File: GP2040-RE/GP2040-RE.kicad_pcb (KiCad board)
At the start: 2 copper layers, 47.5 x 32.9 mm, 38 parts, among them J1 I2C Slave, J2 DEBUG, J3 USB Programming, J4 Console, SW1 BOOTSEL, SW2 RESET, U1 W25Q16JV, U2 RP2040, U3 RT6154AGQW

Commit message: Much happier now
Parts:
- removed SW1: BOOTSEL, Button_Switch_SMD:SW_SPST_B3S-1000
- removed SW2: RESET, Button_Switch_SMD:SW_SPST_B3S-1000
- added J5: RJ-45, RJ-45:CONN8_2-908LF_AMP, F.Cu at (130.3, 101.4)
- added J6: I2C Passthrough, JST-SH:JST_SH_SM04B-SRSS-TB_1x04-1MP_P1.00mm_Horizontal, F.Cu at (146.9, 84.8)
- added J7: Micro_SD_Card, microSD:MEM2061-01-188-00-A_GCT, F.Cu at (126.5, 89.9)
- added J8: Conn_01x10, Connector_PinHeader_2.54mm:PinHeader_1x10_P2.54mm_Vertical, F.Cu at (167.0, 112.3)
- added S1: BOOTSEL, EVP_BB2A9B000:SW_EVP-BB2A9B000, F.Cu at (163.1, 106.5)
- added S2: RESET, EVP_BB2A9B000:SW_EVP-BB2A9B000, F.Cu at (159.4, 106.5)
- J1: footprint Connector_JST:JST_PH_S4B-PH-K_1x04_P2.00mm_Horizontal -> JST-SH:JST_SH_SM04B-SRSS-TB_1x04-1MP_P1.00mm_Horizontal
- J2: footprint Connector_PinHeader_2.54mm:PinHeader_1x03_P2.54mm_Vertical -> JST-SH:JST_SH_SM03B-SRSS-TB_1x03-1MP_P1.00mm_Horizontal
- U1: footprint Package_SO:SOIC-8_5.23x5.23mm_P1.27mm -> W25Q16:USON-8_UX_2x3x0p6_WIN
- moved J2 8.83 mm to (160.4, 111.2), turned to 0 degrees
- moved R1 5.06 mm to (146.1, 93.2)
- moved C2 3.62 mm to (150.7, 92.3)
- moved C1 3.61 mm to (149.9, 92.3)
- moved U1 3.44 mm to (148.7, 94.8)
- moved J1 2.57 mm to (139.1, 84.8)
- moved R5 1.08 mm to (139.3, 88.7)
- moved C8 0.85 mm to (150.8, 98.2)
- moved R4 0.35 mm to (140.9, 88.7)
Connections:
- U2 pad 11: /NES -> unconnected-(U2-GPIO8-Pad11)
- U2 pad 12: /SNES -> unconnected-(U2-GPIO9-Pad12)
- U2 pad 13: /N64 -> unconnected-(U2-GPIO10-Pad13)
- U2 pad 14: /GC -> unconnected-(U2-GPIO11-Pad14)
- U2 pad 16: unconnected-(U2-GPIO13-Pad16) -> /SPI1_CSn
- U2 pad 34: unconnected-(U2-GPIO22-Pad34) -> /OCS
- U2 pad 35: unconnected-(U2-GPIO23-Pad35) -> /RESET
- U2 pad 36: unconnected-(U2-GPIO24-Pad36) -> /Data_Command
- U2 pad 38: unconnected-(U2-GPIO26_ADC0-Pad38) -> /SPI1_SCK
- U2 pad 39: unconnected-(U2-GPIO27_ADC1-Pad39) -> /SPI1_TX_MOSI
- U2 pad 40: unconnected-(U2-GPIO28_ADC2-Pad40) -> /SPI1_RX_MISO
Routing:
- net /CD_gpio: track 13.4 -> 73.7 mm, vias 0 -> 2
- net /CMD_gpio: track 8.56 -> 64.3 mm, vias 0 -> 2
- net /D2_gpio: track 7.20 -> 61.9 mm, vias 0 -> 2
- net /CLK_gpio: track 9.92 -> 64.3 mm, vias 0 -> 2
- net /D1_gpio: track 7.42 -> 61.0 mm, vias 0 -> 2
- net /D0_gpio: track 7.61 -> 61.0 mm, vias 0 -> 2
- net /D3_gpio: track 7.14 -> 58.9 mm, vias 0 -> 2
- net +3.3V: track 96.9 -> 126.4 mm, vias 12 -> 14
- net Net-(R1-Pad1): track 53.9 -> 37.2 mm
- net GND: track 26.6 -> 40.7 mm, vias 12 -> 30
- net /RUN: track 16.1 -> 2.61 mm
- net /SPI1_RX_MISO: track 0.00 -> 12.6 mm, vias 0 -> 1
- net /GreenStripe: track 16.9 -> 27.9 mm
- net /OrangeSolid: track 17.9 -> 27.6 mm
- net /SPI1_TX_MOSI: track 0.00 -> 9.59 mm, vias 0 -> 1
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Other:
- board size 47.5 x 32.9 mm -> 50.8 x 33 mm

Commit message: Now with blinky lights
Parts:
- added D3: LED_Small, LED_SMD:LED_0201_0603Metric, F.Cu at (140.7, 112.8)
- added D4: LED_Small, LED_SMD:LED_0201_0603Metric, F.Cu at (140.7, 113.7)
- added Q1: SBC846BWT1G, SBC846BW:SOT-323-3_2P2X1P35_ONS, F.Cu at (149.0, 111.0)
- added R10: 10k, Resistor_SMD:R_0201_0603Metric, F.Cu at (146.2, 113.7)
- added R11: 10k, Resistor_SMD:R_0201_0603Metric, F.Cu at (142.1, 113.7)
- added R12: 10k, Resistor_SMD:R_0201_0603Metric, F.Cu at (142.1, 112.8)
- added U4: TPS3702CX50DDCR, TPS3702CX50:DDC0006A_N, F.Cu at (145.2, 111.2)
- moved C14 1.62 mm to (148.4, 107.8)
- moved C10 1.59 mm to (150.6, 101.9)
- moved U3 1.47 mm to (145.2, 106.3)
- moved L1 1.46 mm to (145.2, 102.6)
- moved R9 1.13 mm to (142.8, 106.6)
- moved R8 1.12 mm to (142.8, 108.0)
- moved R6 0.96 mm to (148.4, 107.1), turned to 180 degrees
- moved C15 0.69 mm to (148.4, 105.0)
- moved C16 0.69 mm to (148.4, 105.7)
- moved R7 0.69 mm to (148.4, 106.4)
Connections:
- net Net-(D1-Pad1) renamed /InputVoltage
- J8 pad 2: +3.3V -> Net-(J8-Pin_2)
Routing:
- net /CD_gpio: track 73.7 -> 34.2 mm
- net Net-(J8-Pin_2): track 0.00 -> 18.3 mm, vias 0 -> 1
- net VBUS: track 31.0 -> 45.4 mm, vias 1 -> 2
- net /5V_EN: track 0.00 -> 11.0 mm
- net +3.3V: track 126.4 -> 136.6 mm, vias 14 -> 15
- net /InputVoltage: track 6.92 -> 12.1 mm
- net /BrownStripe: track 30.9 -> 34.6 mm
- net /GreenSolid: track 27.3 -> 30.3 mm
- net /BlueStripe: track 28.3 -> 31.3 mm
- net /BlueSolid: track 25.0 -> 27.9 mm
- net GND: track 40.7 -> 43.1 mm, vias 30 -> 34
- net /GreenStripe: track 27.9 -> 29.7 mm
- net Net-(D4-A): track 0.00 -> 0.76 mm
- net Net-(D3-A): track 0.00 -> 0.76 mm
- net Net-(U3-VINA): track 0.96 -> 1.61 mm
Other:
- board size 50.8 x 33 mm -> 50.8 x 33.2 mm

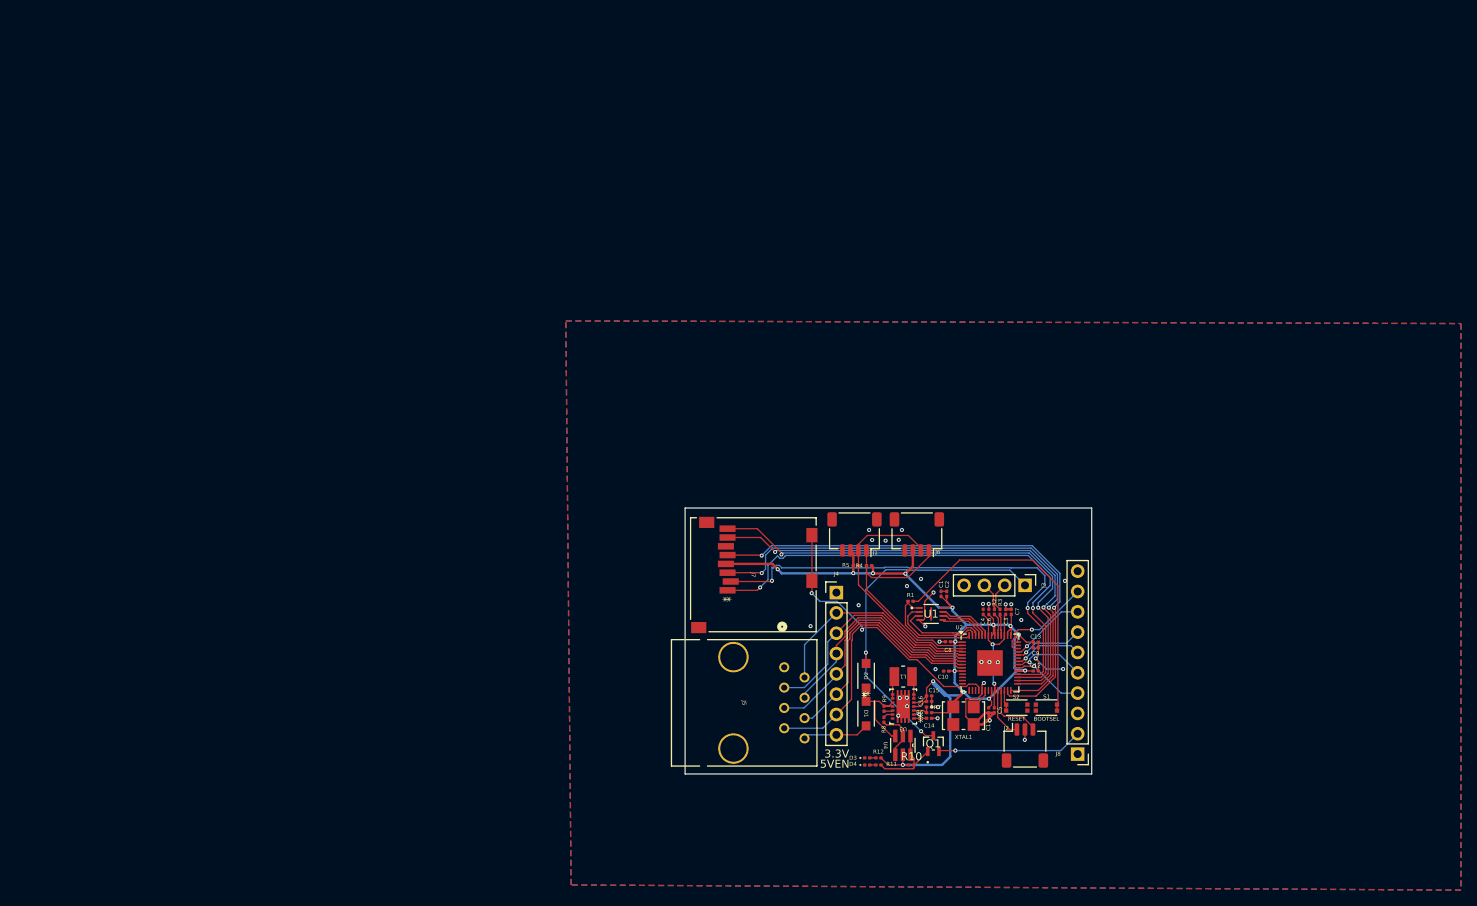
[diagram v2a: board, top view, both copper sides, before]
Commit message: rebuilding part libraries
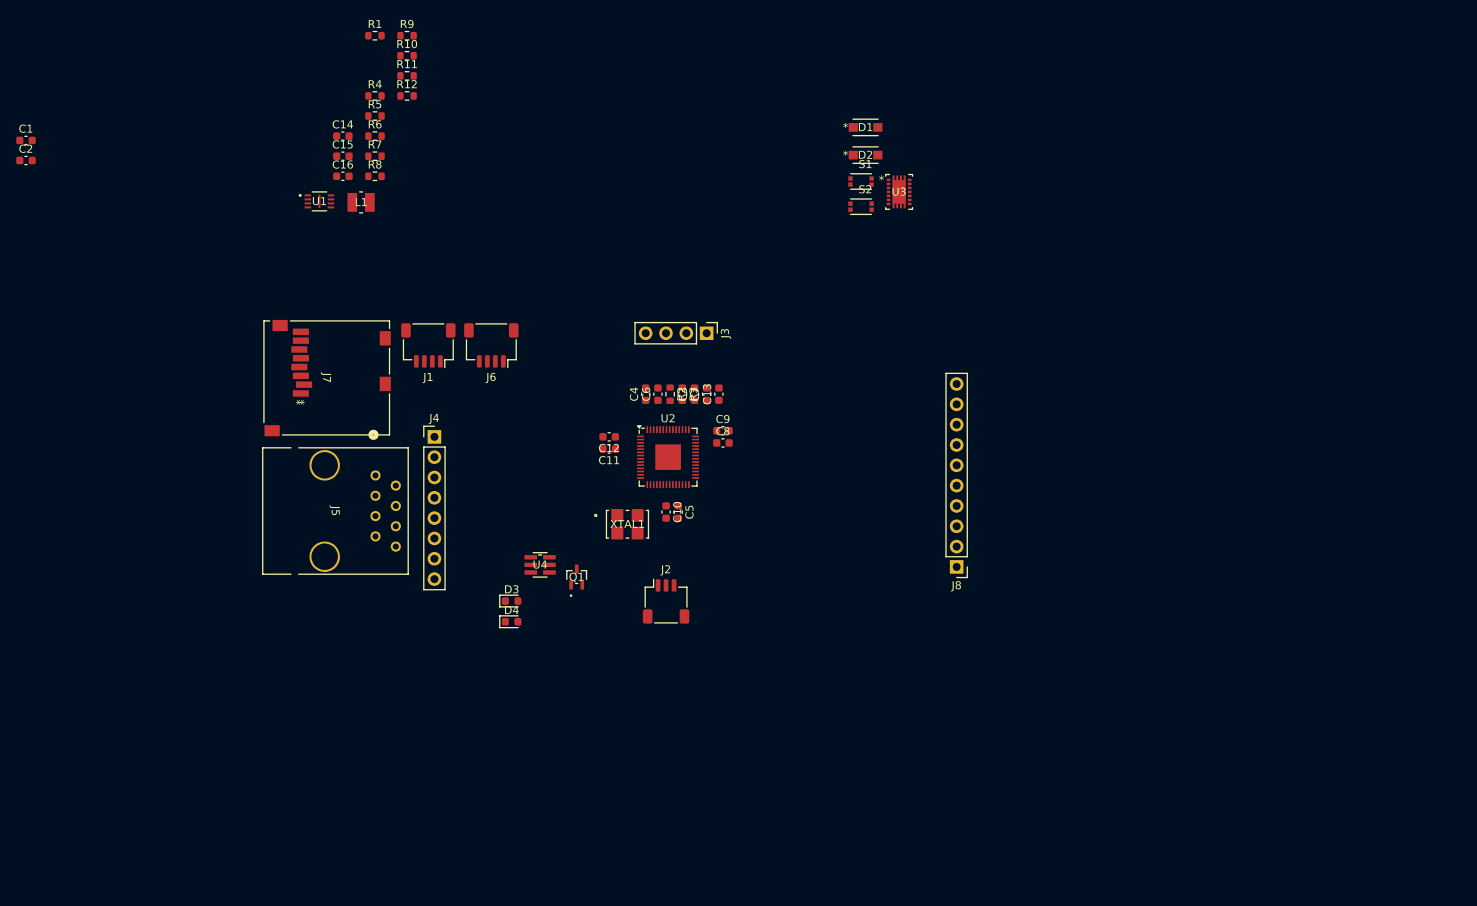
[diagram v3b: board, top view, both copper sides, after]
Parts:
- C1, C10, C11, C12, C13, C14, C15, C16, C2, C3, C4, C5, C6, C7, C8, C9: footprint Capacitor_SMD:C_0201_0603Metric -> Capacitor_SMD:C_0603_1608Metric
- D3, D4: footprint LED_SMD:LED_0201_0603Metric -> LED_SMD:LED_0603_1608Metric
- R1, R10, R11, R12, R2, R3, R4, R5, R6, R7, R8, R9: footprint Resistor_SMD:R_0201_0603Metric -> Resistor_SMD:R_0603_1608Metric
- moved C1 127.7 mm to (35.6, 35.6), turned to 0 degrees
- moved C2 127.2 mm to (35.6, 38.1), turned to 0 degrees
- moved R10 108.8 mm to (83.2, 25.0)
- moved R11 104.4 mm to (83.2, 27.5), turned to 0 degrees
- moved C14 103.3 mm to (75.2, 35.1)
- moved R9 103.1 mm to (83.2, 22.5), turned to 0 degrees
- moved R12 101.6 mm to (83.2, 30.0), turned to 0 degrees
- moved R6 100.0 mm to (79.2, 35.1), turned to 0 degrees
- moved C15 99.6 mm to (75.2, 37.6)
- moved C16 98.4 mm to (75.2, 40.1)
- moved R7 97.7 mm to (79.2, 37.6)
- moved R1 97.4 mm to (79.2, 22.5), turned to 0 degrees
- moved R8 93.1 mm to (79.2, 40.1), turned to 0 degrees
- moved U1 92.2 mm to (72.2, 43.2)
- moved L1 90.0 mm to (77.4, 43.3), turned to 0 degrees
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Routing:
- net +3.3V: track 136.6 -> 0.00 mm, vias 15 -> 0
- net /CLK_gpio: track 64.3 -> 0.00 mm, vias 2 -> 0
- net /CMD_gpio: track 64.3 -> 0.00 mm, vias 2 -> 0
- net /D2_gpio: track 61.9 -> 0.00 mm, vias 2 -> 0
- net /D0_gpio: track 61.0 -> 0.00 mm, vias 2 -> 0
- net /D1_gpio: track 61.0 -> 0.00 mm, vias 2 -> 0
- net /D3_gpio: track 58.9 -> 0.00 mm, vias 2 -> 0
- net VBUS: track 45.4 -> 0.00 mm, vias 2 -> 0
- net GND: track 43.1 -> 0.00 mm, vias 34 -> 0
- net Net-(R1-Pad1): track 37.2 -> 0.00 mm
- net /BrownStripe: track 34.6 -> 0.00 mm
- net /CD_gpio: track 34.2 -> 0.00 mm, vias 2 -> 0
- net /BlueStripe: track 31.3 -> 0.00 mm
- net /SCL: track 30.6 -> 0.00 mm
- net /GreenSolid: track 30.3 -> 0.00 mm
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- removed copper zone on B.Cu, net GND
- removed copper zone on F.Cu, net GND
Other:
- board outline removed
- copper layers 2 -> 4
- rule pad_to_mask_clearance: 0.0508 -> 0.0381

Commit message: 4 Layer board
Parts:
- removed U3: RT6154AGQW, RT6154A:QFN_4AGQW_RIT
- added C17: 47u 6.3V X5R 20%, Capacitor_SMD:C_0603_1608Metric, F.Cu at (67.1, 73.7)
- added C18: 47u 6.3V X5R 20%, Capacitor_SMD:C_0603_1608Metric, F.Cu at (61.5, 72.9)
- added R13: 27 50mW 1% M0603, Resistor_SMD:R_0603_1608Metric, F.Cu at (81.5, 60.5)
- added U5: TPS3702CX50DDCR, GP2040-RE:DDC0006A_N, F.Cu at (64.3, 65.8)
- C1: value 2.2u 6.3v 20% -> 2.2u 6.3V X5R 20%
- C10, C11, C2, C4, C5, C6, C8, C9: value 100n 6.3V 10% -> 100n 6.3V X5R 10%
- C12, C13, C14: value 100n 6.3V 10% -> 2.2u 6.3V X5R 20%
- C15: value 47u 6.3V 20% -> 100n 6.3V X5R 10%
- C16: value 47u 6.3V 20% -> 47u 6.3V X5R 20%
- C3, C7: value 1uF -> 100n 6.3V X5R 10%
- D1, D2: value MBR120VLSFT1G -> LED_Small; footprint MBR120V:SDO_SOD-123FL_ONS -> LED_SMD:LED_0603_1608Metric
- D3, D4: value LED_Small -> 20V 1A; footprint LED_SMD:LED_0603_1608Metric -> GP2040-RE:SDO_SOD-123FL_ONS
- J1: value I2C Slave -> I2C Target; footprint JST-SH:JST_SH_SM04B-SRSS-TB_1x04-1MP_P1.00mm_Horizontal -> GP2040-RE:CONN_SM04B-SRSS-TB_JST
- J2: value DEBUG -> I2C Controller; footprint JST-SH:JST_SH_SM03B-SRSS-TB_1x03-1MP_P1.00mm_Horizontal -> GP2040-RE:CONN_SM04B-SRSS-TB_JST
- J3: value USB Programming -> SM03B-SRSS-TB_LF__SN_; footprint Connector_PinHeader_2.54mm:PinHeader_1x04_P2.54mm_Vertical -> GP2040-RE:JST_SM03B-SRSS-TB_LF__SN_
- J4: value Console -> USB Programming; footprint Connector_PinHeader_2.54mm:PinHeader_1x08_P2.54mm_Vertical -> Connector_PinHeader_2.54mm:PinHeader_1x04_P2.54mm_Vertical
- J5: value RJ-45 -> Conn_01x03; footprint RJ-45:CONN8_2-908LF_AMP -> Connector_PinHeader_2.54mm:PinHeader_1x03_P2.54mm_Vertical
- J6: value I2C Passthrough -> microSD; footprint JST-SH:JST_SH_SM04B-SRSS-TB_1x04-1MP_P1.00mm_Horizontal -> GP2040-RE:MEM2061-01-188-00-A_GCT
- J7: value Micro_SD_Card -> RJ-45; footprint microSD:MEM2061-01-188-00-A_GCT -> GP2040-RE:CONN8_2-908LF_AMP
- L1: value 1uH -> SRN2512-1R0M; footprint SRN2512:IND_SRN2512_BRN -> GP2040-RE:IND_SRN2512_BRN
- Q1: value SBC846BWT1G -> NPN 65V 0.1A; footprint SBC846BW:SOT-323-3_2P2X1P35_ONS -> GP2040-RE:SOT-323-3_2P2X1P35_ONS
- R11: value 10k -> VREF SHUNT 2%; footprint Resistor_SMD:R_0603_1608Metric -> GP2040-RE:DBZ3
- R12: value 10k -> 27 50mW 1% M0603
- R2, R3: value 27 50mW 1% -> 4.7k
- R4, R5: value 4.7k -> 10k
- R6: value 560K 50mW 1% -> 100K 50mW 1%
- R8: value 100K 50mW 1% -> 560K 50mW 1%
- S1: value BOOTSEL -> Buttons; footprint EVP_BB2A9B000:SW_EVP-BB2A9B000 -> GP2040-RE:SW_EVP-BB2A9B000
- S2: value RESET -> Buttons; footprint EVP_BB2A9B000:SW_EVP-BB2A9B000 -> GP2040-RE:SW_EVP-BB2A9B000
- U1: value W25Q16JV -> RP2040; footprint W25Q16:USON-8_UX_2x3x0p6_WIN -> GP2040-RE:QFN56_7X7_RPI
- U2: value RP2040 -> 16M; footprint Package_DFN_QFN:QFN-56-1EP_7x7mm_P0.4mm_EP3.2x3.2mm -> GP2040-RE:USON-8_UX_2x3x0p6_WIN
- U4: value TPS3702CX50DDCR -> Linear Regulator; footprint TPS3702CX50:DDC0006A_N -> GP2040-RE:QFN_4AGQW_RIT
- XTAL1: footprint SIT1602:SON4_SIT1602-3_SIT -> GP2040-RE:SON4_SIT1602-3_SIT
- moved J8 86.4 mm to (74.4, 50.5), turned to 90 degrees
- moved J2 62.9 mm to (68.4, 51.6)
- moved S1 60.4 mm to (93.5, 79.2), turned to 90 degrees
- moved S2 60.2 mm to (91.2, 79.2), turned to 90 degrees
- moved R3 59.1 mm to (59.7, 55.6), turned to 180 degrees
- moved R9 57.6 mm to (68.6, 78.2), turned to -90 degrees
- moved R2 54.6 mm to (62.7, 55.6), turned to 0 degrees
- moved D1 47.8 mm to (97.5, 54.9), turned to 180 degrees
- moved R6 46.7 mm to (61.5, 78.2), turned to 180 degrees
- moved C3 46.6 mm to (74.2, 79.8), turned to -90 degrees
- moved J6 46.3 mm to (47.8, 56.1), turned to -90 degrees
- moved D2 45.8 mm to (97.5, 53.3), turned to 180 degrees
- moved C5 45.6 mm to (72.4, 73.2), turned to 180 degrees
- moved C1 45.0 mm to (72.4, 61.5), turned to 90 degrees
- moved C2 44.9 mm to (73.9, 61.5), turned to 90 degrees
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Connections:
- C11 pad 1: +3.3V -> +1V1
- C12 pad 1: +3.3V -> +1V1
- C14 pad 1: Net-(U3-VINA) -> +3.3V
- C15 pad 1: +3.3V -> Net-(U4-VINA)
- C3 pad 1: +1V1 -> +3.3V
- C4 pad 1: +1V1 -> +3.3V
- C5 pad 1: +1V1 -> +3.3V
- C9 pad 1: +3.3V -> +1V1
- D1 pad 1: /InputVoltage -> GND
- D1 pad 2: /BrownSolid -> Net-(D1-A)
- D2 pad 1: /InputVoltage -> GND
- D2 pad 2: VBUS -> Net-(D2-A)
- D3 pad 1: GND -> /InputVoltage
- D3 pad 2: Net-(D3-A) -> /OrangeSolid
- D4 pad 1: GND -> /InputVoltage
- D4 pad 2: Net-(D4-A) -> VBUS
- J1 pad 1: /SDA -> /SDA_0
- J1 pad 2: /SCL -> /SCL_0
- J2 pad 1: /SWCLK -> /SDA_1
- J2 pad 2: GND -> /SCL_1
- J2 pad 3: /SWDIO -> +3.3V
- J3 pad 1: VBUS -> /SWCLK
- J3 pad 2: /D- -> GND
- J3 pad 3: /D+ -> /SWDIO
- J4 pad 1: GND -> VBUS
- J4 pad 2: /OrangeSolid -> /D-
- J4 pad 3: /GreenStripe -> /D+
- J4 pad 4: /BlueSolid -> GND
- J5 pad 1: GND -> /UART_RX
- J5 pad 2: /OrangeSolid -> /UART_TX
- J5 pad 3: /GreenStripe -> GND
- J7 pad 10: /CD_gpio -> (no net)
- J7 pad 9: /CD_gpio -> (no net)
- Q1 pad 2: Net-(J8-Pin_2) -> VBUS
- Q1 pad 3: VBUS -> Net-(J8-Pin_2)
- R11 pad 1: /5V_EN -> +3.3V
- R11 pad 2: Net-(D4-A) -> GND
- R12 pad 1: +3.3V -> /+
- R12 pad 2: Net-(D3-A) -> /D+
- R2 pad 1: /D+ -> /SDA_0
- R2 pad 2: /+ -> +3.3V
- R3 pad 1: /D- -> /SCL_0
- R3 pad 2: /- -> +3.3V
- R4 pad 1: /SDA -> +3.3V
- R4 pad 2: +3.3V -> Net-(D1-A)
- R5 pad 1: +3.3V -> /5V_EN
- R5 pad 2: /SCL -> Net-(D2-A)
- R6 pad 1: +3.3V -> Net-(U4-PS/SYNC)
- R6 pad 2: Net-(U3-FB) -> GND
- R7 pad 1: Net-(U3-FB) -> Net-(U4-EN)
- R7 pad 2: GND -> /InputVoltage
- R8 pad 1: Net-(U3-PS/SYNC) -> +3.3V
- R8 pad 2: GND -> Net-(U4-FB)
- R9 pad 1: Net-(U3-EN) -> Net-(U4-FB)
- R9 pad 2: /InputVoltage -> GND
- U1 pad 1: /QSPI_SS -> +3.3V
- U1 pad 2: /QSPI_SD1 -> /UART_TX
- U1 pad 3: /QSPI_SD2 -> /UART_RX
- U1 pad 4: GND -> /GreenStripe
- U1 pad 5: /QSPI_SD0 -> /BlueSolid
- U1 pad 6: /QSPI_SCLK -> /BlueStripe
- U1 pad 7: /QSPI_SD3 -> /GreenSolid
- U1 pad 8: +3.3V -> /BrownStripe
- U1 pad 9: (no net) -> /BrownSolid
- U2 pad 1: +3.3V -> /QSPI_SS
- U2 pad 2: /SDA -> /QSPI_SD1
- U2 pad 3: /SCL -> /QSPI_SD2
- U2 pad 4: /OrangeSolid -> GND
- U2 pad 5: /GreenStripe -> /QSPI_SD0
- U2 pad 6: /BlueSolid -> /QSPI_SCLK
- U2 pad 7: /BlueStripe -> /QSPI_SD3
- U2 pad 8: /GreenSolid -> +3.3V
- U2 pad 9: /BrownStripe -> (no net)
- U4 pad 1: /5V_EN -> Net-(U4-VINA)
- U4 pad 3: /InputVoltage -> Net-(U4-FB)
- U4 pad 4: GND -> +3.3V
- U4 pad 6: /5V_EN -> Net-(L1-Pad1)
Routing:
- net /CLK_gpio: track 0.00 -> 76.8 mm, vias 0 -> 2
- net /D1_gpio: track 0.00 -> 74.7 mm, vias 0 -> 2
- net GND: track 0.00 -> 73.7 mm, vias 0 -> 57
- net /D0_gpio: track 0.00 -> 71.7 mm, vias 0 -> 2
- net /CMD_gpio: track 0.00 -> 71.4 mm, vias 0 -> 2
- net /CD_gpio: track 0.00 -> 67.0 mm, vias 0 -> 5
- net /D2_gpio: track 0.00 -> 67.0 mm, vias 0 -> 2
- net /SCL_0: track 0.00 -> 65.2 mm, vias 0 -> 2
- net /D3_gpio: track 0.00 -> 65.1 mm, vias 0 -> 2
- net +3.3V: track 0.00 -> 62.7 mm, vias 0 -> 17
- net /SDA_0: track 0.00 -> 61.6 mm, vias 0 -> 2
- net /SPI1_RX_MISO: track 0.00 -> 58.1 mm, vias 0 -> 1
- net /SPI1_TX_MOSI: track 0.00 -> 57.1 mm, vias 0 -> 1
- net /SPI1_SCK: track 0.00 -> 56.7 mm, vias 0 -> 1
- net /Data_Command: track 0.00 -> 53.9 mm, vias 0 -> 1
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- added copper zone on In2.Cu, net +3.3V
- added copper zone on In1.Cu, net GND
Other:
- board outline added: 63.2 x 36.1 mm
